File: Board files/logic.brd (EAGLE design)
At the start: 44.1 x 57.1 mm, 19 parts, among them U2 LD1117, U3 LM2662

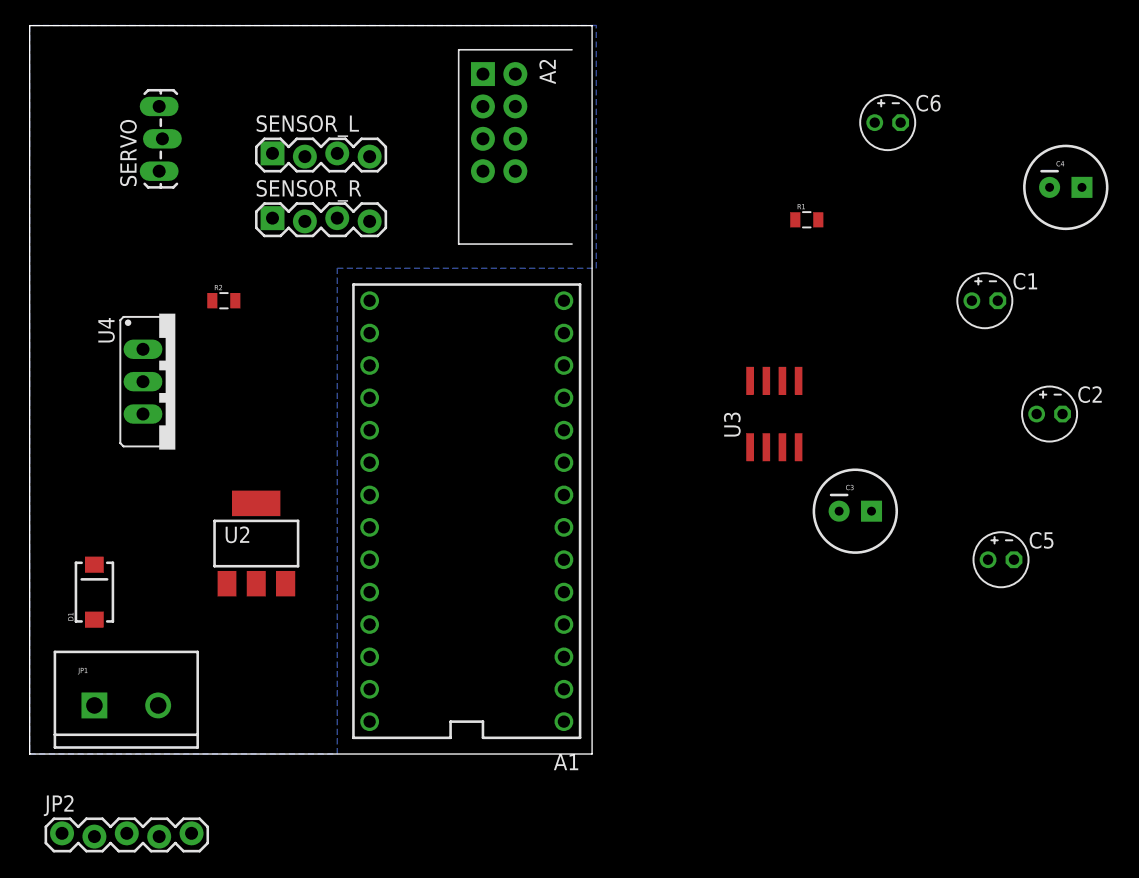
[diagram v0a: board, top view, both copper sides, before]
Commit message: Finished logic board layout
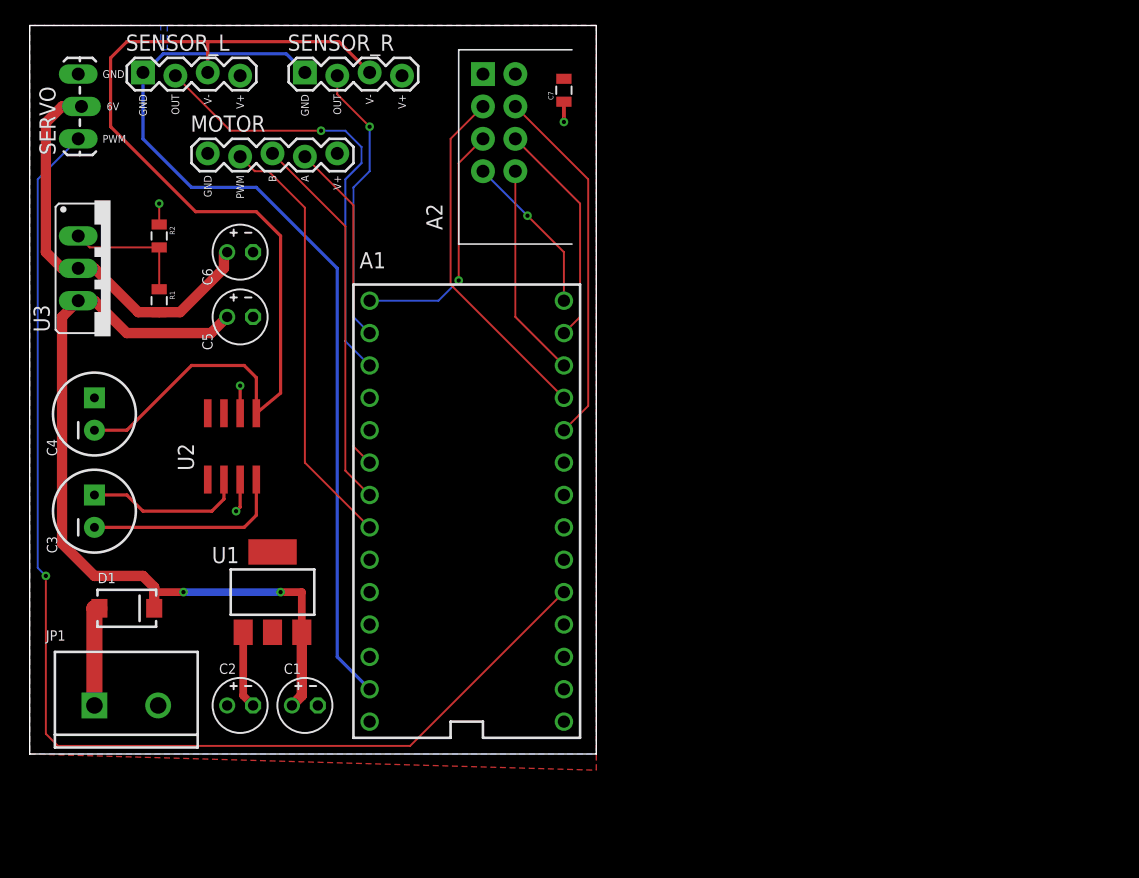
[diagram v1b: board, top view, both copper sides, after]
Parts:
- removed JP2: (no value), SparkFun-Connectors:1X05_LOCK
- removed U4: (no value), v-reg:317TS
- added C7: 0.1uF, SparkFun-Capacitors:0805
- added MOTOR: (no value), SparkFun-Connectors:1X05_LOCK
- added U1: LD1117, Custom:SOT-223
- C1, C2, C5, C6: value (none) -> 10uF
- C3, C4: value (none) -> 47uF
- U2: value LD1117 -> LM2662; device Custom:SOT-223 -> Custom:SOIC-8
- U3: value LM2662 -> LD1085V; device Custom:SOIC-8 -> v-reg:317TS
- moved C4 78.2 mm to (5.08, 26.7), turned to 90 degrees
- moved C2 67.5 mm to (16.5, 3.81)
- moved C5 62.7 mm to (16.5, 34.3)
- moved C1 62.1 mm to (21.6, 3.81)
- moved C3 59.7 mm to (5.08, 19.1), turned to 90 degrees
- moved U3 53.3 mm to (6.35, 38.1), turned to 270 degrees
- moved C6 51.8 mm to (16.5, 39.4)
- moved R1 51.2 mm to (10.2, 35.6), turned to 270 degrees
- moved SENSOR_L 12.0 mm to (8.89, 53.3)
- moved SENSOR_R 11.7 mm to (21.6, 53.3)
- moved U2 7.85 mm to (15.9, 24.1)
- moved R2 7.18 mm to (10.2, 40.6), turned to 270 degrees
- moved SERVO 6.84 mm to (3.81, 48.3)
- moved D1 2.84 mm to (7.62, 11.4), turned to 0 degrees
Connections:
- new net N$17: A1.18/A4, MOTOR.4
- net 3.3V: now also C7.2, MOTOR.5, U1.2, U1.4, U2.8; no longer JP2.5, U2.2, U2.4, U3.8
- net 6V: now also U3.2; no longer U4.2
- net GND: now also C7.1, MOTOR.1, U1.1, U2.3, U2.6; no longer A1.AGND, JP2.1, SENSOR_L.1, SENSOR_R.1, U2.1, U3.3, U3.6
- net N$10: now also A1.9; no longer A1.14/A0
- net N$12: now also A1.AGND, SENSOR_L.1, SENSOR_R.1; no longer A1.16/A2, SENSOR_R.2
- net N$13: now also A1.15/A1; no longer A1.17/A3
- net N$14: now also A1.14/A0, SENSOR_R.2; no longer A1.5, JP2.2
- net N$15: now also A1.20/A6, MOTOR.2; no longer A1.6, JP2.4
- net N$16: now also A1.19/A5, MOTOR.3; no longer A1.7, JP2.3
- net N$2: now also U2.2; no longer U3.2
- net N$3: now also U2.4; no longer U3.4
- net N$4: now also U3.1; no longer U4.1
- net N$8: now also A1.8; no longer A1.10
- net N$9: now also A1.10; no longer A1.15/A1
- net VNEG: now also U2.5; no longer U3.5
- net V_BATT: now also U1.3, U3.3; no longer U2.3, U4.3
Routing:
- net N$11: track 0.00 -> 94.3 mm, vias 0 -> 1
- net VNEG: track 0.00 -> 79.3 mm
- net N$12: track 0.00 -> 72.6 mm
- net V_BATT: track 0.00 -> 63.9 mm, vias 0 -> 2
- net N$13: track 0.00 -> 35.4 mm, vias 0 -> 1
- net N$15: track 0.00 -> 33.9 mm
- net 6V: track 0.00 -> 32.3 mm
- net N$16: track 0.00 -> 30.0 mm
- net N$8: track 0.00 -> 28.6 mm
- net N$10: track 0.00 -> 27.6 mm
- net N$17: track 0.00 -> 26.1 mm
- net N$14: track 0.00 -> 22.3 mm, vias 0 -> 1
- net N$5: track 0.00 -> 19.5 mm, vias 0 -> 1
- net N$7: track 0.00 -> 17.9 mm
- net N$9: track 0.00 -> 16.8 mm
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- added copper zone on layer 1, net 3.3V
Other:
- board size 44.1 x 57.1 mm -> 44.5 x 57.1 mm
- board text added: "6V"
- board text added: "A"
- board text added: "B"
- board text added: "GND"
- board text added: "OUT"
- board text added: "PWM"
- board text added: "V+"
- board text added: "V-"

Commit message: Rerouted servo trace and added labels
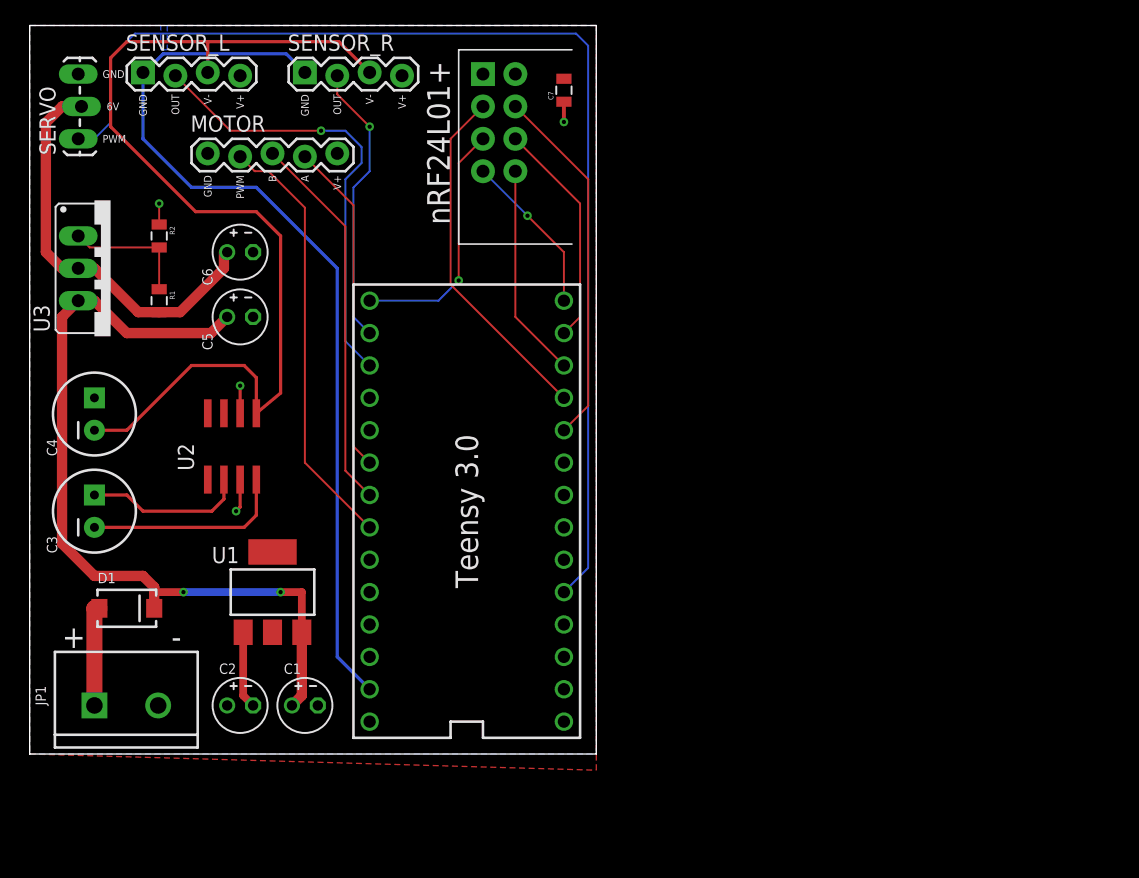
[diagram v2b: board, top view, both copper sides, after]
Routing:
- net N$11: track 94.3 -> 90.4 mm, vias 1 -> 0
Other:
- board text added: "+"
- board text added: "-"
- board text added: "Teensy 3.0"
- board text added: "nRF24L01+"
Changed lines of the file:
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@@
 <text x="26.67" y="51.7525" size="0.6096" layer="21" rot="R270" align="center-left">V-</text>
 <text x="29.21" y="51.7525" size="0.6096" layer="21" rot="R270" align="center-left">V+</text>
+<text x="2.54" y="9.2075" size="1.778" layer="21" align="center-left">+</text>
+<text x="11.1125" y="9.2075" size="1.778" layer="21" align="center-left">-</text>
+<text x="34.29" y="19.05" size="1.778" layer="21" rot="R90" align="center">Teensy 3.0</text>
+<text x="32.0675" y="47.9425" size="1.778" layer="21" rot="R90" align="center">nRF24L01+</text>
 </plain>
 <attributes>
@@
 </element>
 <element name="JP1" library="SparkFun-Connectors" package="SCREWTERMINAL-5MM-2" value="M025MM" x="5.08" y="3.81" smashed="yes">
-<attribute name="NAME" x="1.27" y="8.89" size="0.8128" layer="25"/>
+<attribute name="NAME" x="1.27" y="3.81" size="0.8128" layer="25" rot="R90"/>
 </element>
 <element name="U3" library="v-reg" package="317TS" value="LD1085V" x="6.35" y="38.1" smashed="yes" rot="R270">
@@
 <attribute name="NAME" x="14.351" y="36.7665" size="0.8128" layer="25" ratio="10" rot="R90"/>
 </element>
-<element name="A2" library="Custom" package="NRF24L01+" value="NRF24L01+" x="36.83" y="49.53" smashed="yes" rot="R270">
-<attribute name="NAME" x="31.115" y="43.18" size="1.27" layer="25" ratio="10" rot="R270"/>
-</element>
-<element name="A1" library="Teensy3.0" package="TEENSY_3.0_SIDES" value="TEENSY_3.0_SIDES" x="34.29" y="19.05" smashed="yes" rot="R180">
-<attribute name="NAME" x="27.94" y="39.37" size="1.27" layer="25" font="vector" rot="R180"/>
-</element>
+<element name="A2" library="Custom" package="NRF24L01+" value="NRF24L01+" x="36.83" y="49.53" smashed="yes" rot="R270"/>
+<element name="A1" library="Teensy3.0" package="TEENSY_3.0_SIDES" value="TEENSY_3.0_SIDES" x="34.29" y="19.05" smashed="yes" rot="R180"/>
 <element name="SERVO" library="SparkFun-Connectors" package="1X03_LOCK_LONGPADS" value="" x="3.81" y="48.26" smashed="yes" rot="R90">
 <attribute name="NAME" x="2.032" y="46.99" size="1.27" layer="25" font="vector" ratio="10" rot="R90"/>
@@
 <contactref element="SERVO" pad="1"/>
 <contactref element="A1" pad="3"/>
-<wire x1="3.81" y1="48.26" x2="0.635" y2="45.085" width="0.1524" layer="16"/>
-<wire x1="0.635" y1="45.085" x2="0.635" y2="14.605" width="0.1524" layer="16"/>
-<wire x1="0.635" y1="14.605" x2="1.27" y2="13.97" width="0.1524" layer="16"/>
-<via x="1.27" y="13.97" extent="1-16" drill="0.3302"/>
-<wire x1="1.27" y1="13.97" x2="1.27" y2="1.5875" width="0.1524" layer="1"/>
-<wire x1="1.27" y1="1.5875" x2="2.2225" y2="0.635" width="0.1524" layer="1"/>
-<wire x1="2.2225" y1="0.635" x2="29.845" y2="0.635" width="0.1524" layer="1"/>
-<wire x1="29.845" y1="0.635" x2="41.91" y2="12.7" width="0.1524" layer="1"/>
+<wire x1="41.91" y1="12.7" x2="43.815" y2="14.605" width="0.1524" layer="16"/>
+<wire x1="43.815" y1="14.605" x2="43.815" y2="55.5625" width="0.1524" layer="16"/>
+<wire x1="43.815" y1="55.5625" x2="42.8625" y2="56.515" width="0.1524" layer="16"/>
+<wire x1="42.8625" y1="56.515" x2="8.255" y2="56.515" width="0.1524" layer="16"/>
+<wire x1="8.255" y1="56.515" x2="6.35" y2="54.61" width="0.1524" layer="16"/>
+<wire x1="6.35" y1="54.61" x2="6.35" y2="49.53" width="0.1524" layer="16"/>
+<wire x1="6.35" y1="49.53" x2="5.08" y2="48.26" width="0.1524" layer="16"/>
+<wire x1="5.08" y1="48.26" x2="3.81" y2="48.26" width="0.1524" layer="16"/>
 </signal>
 <signal name="N$6">

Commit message: Changed logic board layout
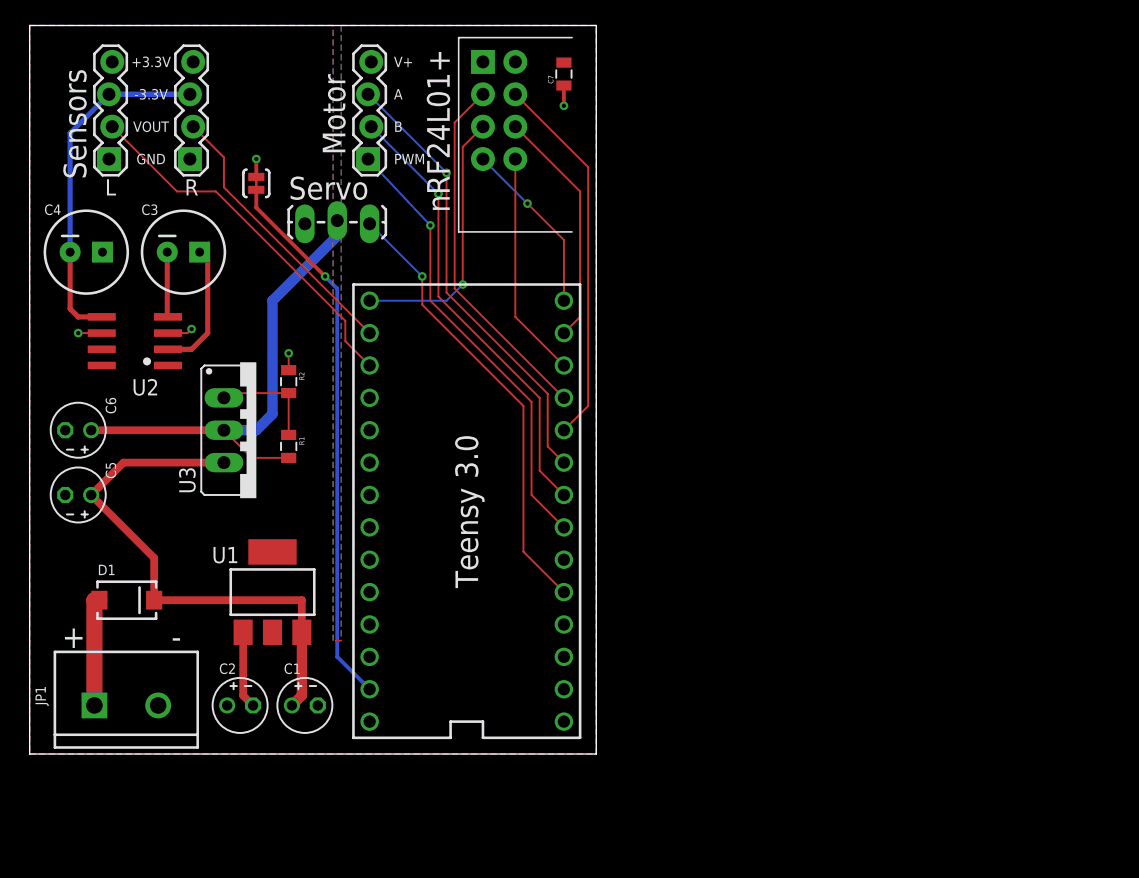
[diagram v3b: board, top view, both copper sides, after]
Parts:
- added SJ1: SOLDERJUMPERTRACE, SparkFun-Passives:SJ_2S-TRACE
- MOTOR: device SparkFun-Connectors:1X05_LOCK -> SparkFun-Connectors:1X04_LOCK
- moved SERVO 23.8 mm to (26.7, 41.6), turned to 180 degrees
- moved C3 21.5 mm to (12.1, 39.4), turned to 0 degrees
- moved C5 18.9 mm to (3.81, 20.3), turned to 180 degrees
- moved C6 18.9 mm to (3.81, 25.4), turned to 180 degrees
- moved U3 17.1 mm to (17.8, 25.4)
- moved R1 15.3 mm to (20.3, 24.1)
- moved R2 15.3 mm to (20.3, 29.2)
- moved C4 12.7 mm to (4.45, 39.4), turned to 0 degrees
- moved MOTOR 12.7 mm to (26.7, 46.7), turned to 90 degrees
- moved U2 11.2 mm to (8.26, 32.4), turned to 90 degrees
- moved SENSOR_R 11.1 mm to (12.7, 46.7), turned to 90 degrees
- moved SENSOR_L 7.13 mm to (6.35, 46.7), turned to 90 degrees
- moved C7 1.27 mm to (41.9, 53.3)
- moved A2 0.95 mm to (36.8, 50.5)
- moved D1 0.63 mm to (7.62, 12.1)
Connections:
- net 3.3V: now also MOTOR.4; no longer MOTOR.5
- net GND: now also SENSOR_L.1, SENSOR_R.1, SJ1.2; no longer MOTOR.1
- net N$12: now also SJ1.1; no longer SENSOR_L.1, SENSOR_R.1
- net N$15: now also A1.5, MOTOR.1; no longer A1.20/A6, MOTOR.2
- net N$16: now also A1.6, MOTOR.2; no longer A1.19/A5, MOTOR.3
- net N$17: now also A1.7, MOTOR.3; no longer A1.18/A4, MOTOR.4
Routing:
- net N$11: track 90.4 -> 35.2 mm, vias 0 -> 1
- net VNEG: track 79.3 -> 27.2 mm
- net N$12: track 72.6 -> 42.9 mm, vias 0 -> 1
- net V_BATT: track 63.9 -> 42.6 mm, vias 2 -> 0
- net N$3: track 15.9 -> 5.10 mm
- net N$17: track 26.1 -> 35.3 mm, vias 0 -> 1
- net N$13: track 35.4 -> 28.9 mm, vias 1 -> 0
- net 6V: track 32.3 -> 38.0 mm
- net N$16: track 30.0 -> 35.2 mm, vias 0 -> 1
- net N$2: track 12.6 -> 10.3 mm
- net N$4: track 10.0 -> 8.51 mm
- net N$5: track 19.5 -> 20.9 mm
- net N$15: track 33.9 -> 35.2 mm, vias 0 -> 1
- net N$9: track 16.8 -> 17.8 mm
- net N$8: track 28.6 -> 29.5 mm
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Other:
- board text added: "+3.3V"
- board text added: "-3.3V"
- board text added: "L"
- board text added: "Motor"
- board text added: "R"
- board text added: "Sensors"
- board text added: "Servo"
- board text added: "VOUT"
- board text removed: "6V"
- board text removed: "OUT"
- board text removed: "V-"

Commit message: More logic board edits
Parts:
- moved U1 1.27 mm to (17.8, 12.7)
- moved C5 0.95 mm to (3.81, 21.3)
- moved C6 0.64 mm to (3.81, 26.0)
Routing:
- net V_BATT: track 42.6 -> 40.3 mm
- net GND: track 14.2 -> 14.7 mm
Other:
- board text added: "3.3V"
- board text removed: "V+"
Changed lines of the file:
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@@
 <text x="28.575" y="49.2125" size="0.8128" layer="21" align="center-left">B</text>
 <text x="28.575" y="51.7525" size="0.8128" layer="21" align="center-left">A</text>
-<text x="28.575" y="54.2925" size="0.8128" layer="21" align="center-left">V+</text>
+<text x="28.575" y="54.2925" size="0.8128" layer="21" align="center-left">3.3V</text>
 <text x="2.54" y="9.2075" size="1.778" layer="21" align="center-left">+</text>
 <text x="11.1125" y="9.2075" size="1.778" layer="21" align="center-left">-</text>
@@
 <attribute name="VALUE" x="7.874" y="13.716" size="0.4064" layer="27"/>
 </element>
-<element name="U1" library="Custom" package="SOT-223" value="LD1117" x="19.05" y="12.7" smashed="yes">
-<attribute name="NAME" x="14.2875" y="14.9733" size="1.27" layer="25"/>
+<element name="U1" library="Custom" package="SOT-223" value="LD1117" x="17.78" y="12.7" smashed="yes">
+<attribute name="NAME" x="13.0175" y="14.9733" size="1.27" layer="25"/>
 </element>
 <element name="JP1" library="SparkFun-Connectors" package="SCREWTERMINAL-5MM-2" value="M025MM" x="5.08" y="3.81" smashed="yes">
@@
 <attribute name="NAME" x="14.859" y="6.2865" size="0.8128" layer="25" ratio="10"/>
 </element>
-<element name="C5" library="resistor" package="E2-4" value="10uF" x="3.81" y="20.32" smashed="yes" rot="R180">
-<attribute name="NAME" x="5.969" y="22.9235" size="0.8128" layer="25" ratio="10" rot="R270"/>
-</element>
-<element name="C6" library="resistor" package="E2-4" value="10uF" x="3.81" y="25.4" smashed="yes" rot="R180">
-<attribute name="NAME" x="5.969" y="28.0035" size="0.8128" layer="25" ratio="10" rot="R270"/>
+<element name="C5" library="resistor" package="E2-4" value="10uF" x="3.81" y="21.2725" smashed="yes" rot="R180">
+<attribute name="NAME" x="5.969" y="23.876" size="0.8128" layer="25" ratio="10" rot="R270"/>
+</element>
+<element name="C6" library="resistor" package="E2-4" value="10uF" x="3.81" y="26.035" smashed="yes" rot="R180">
+<attribute name="NAME" x="5.969" y="28.6385" size="0.8128" layer="25" ratio="10" rot="R270"/>
 </element>
 <element name="A2" library="Custom" package="NRF24L01+" value="NRF24L01+" x="36.83" y="50.4825" smashed="yes" rot="R270"/>
@@
 <vertex x="0" y="57.15"/>
 </polygon>
-<wire x1="16.75" y1="9.55" x2="16.75" y2="4.586" width="0.6096" layer="1"/>
-<wire x1="16.75" y1="4.586" x2="17.526" y2="3.81" width="0.6096" layer="1"/>
 <contactref element="A2" pad="1"/>
 <contactref element="C7" pad="1"/>
@@
 <wire x1="17.78" y1="45.2755" x2="17.78" y2="46.6725" width="0.3048" layer="1"/>
 <via x="17.78" y="46.6725" extent="1-16" drill="0.3302"/>
+<wire x1="15.48" y1="9.55" x2="15.48" y2="7.38" width="0.6096" layer="1"/>
+<wire x1="15.48" y1="7.38" x2="17.526" y2="5.334" width="0.6096" layer="1"/>
+<wire x1="17.526" y1="5.334" x2="17.526" y2="3.81" width="0.6096" layer="1"/>
 </signal>
 <signal name="3.3V">
@@
 <contactref element="C1" pad="+"/>
 <contactref element="C5" pad="+"/>
-<wire x1="21.35" y1="9.55" x2="21.35" y2="8.89" width="0.8128" layer="1"/>
-<wire x1="21.35" y1="8.89" x2="21.35" y2="4.586" width="0.8128" layer="1"/>
-<wire x1="21.35" y1="4.586" x2="20.574" y2="3.81" width="0.8128" layer="1"/>
-<wire x1="9.77" y1="12.065" x2="9.77" y2="15.376" width="0.6096" layer="1"/>
-<wire x1="9.77" y1="15.376" x2="4.826" y2="20.32" width="0.6096" layer="1"/>
-<wire x1="15.24" y1="22.86" x2="7.366" y2="22.86" width="0.6096" layer="1"/>
-<wire x1="7.366" y1="22.86" x2="4.826" y2="20.32" width="0.6096" layer="1"/>
-<wire x1="9.77" y1="12.065" x2="21.35" y2="12.065" width="0.6096" layer="1"/>
-<wire x1="21.35" y1="12.065" x2="21.35" y2="8.89" width="0.6096" layer="1"/>
+<wire x1="9.77" y1="12.065" x2="9.77" y2="16.3285" width="0.8128" layer="1"/>
+<wire x1="20.08" y1="9.55" x2="20.08" y2="4.304" width="0.6096" layer="1"/>
+<wire x1="20.08" y1="4.304" x2="20.574" y2="3.81" width="0.6096" layer="1"/>
+<wire x1="9.77" y1="12.065" x2="18.415" y2="12.065" width="0.6096" layer="1"/>
+<wire x1="18.415" y1="12.065" x2="20.32" y2="10.16" width="0.6096" layer="1"/>
+<wire x1="20.32" y1="10.16" x2="20.32" y2="9.79" width="0.6096" layer="1"/>
+<wire x1="20.32" y1="9.79" x2="20.08" y2="9.55" width="0.6096" layer="1"/>
+<wire x1="9.77" y1="16.3285" x2="4.826" y2="21.2725" width="0.8128" layer="1"/>
+<wire x1="4.826" y1="21.2725" x2="13.6525" y2="21.2725" width="0.8128" layer="1"/>
+<wire x1="13.6525" y1="21.2725" x2="15.24" y2="22.86" width="0.8128" layer="1"/>
 </signal>
 <signal name="N$1">
@@
 <wire x1="20.32" y1="23.23" x2="17.41" y2="23.23" width="0.1524" layer="1"/>
 <wire x1="17.41" y1="23.23" x2="15.24" y2="25.4" width="0.1524" layer="1"/>
-<wire x1="4.826" y1="25.4" x2="15.24" y2="25.4" width="0.6096" layer="1"/>
+<wire x1="4.826" y1="26.035" x2="5.461" y2="25.4" width="0.8128" layer="1"/>
+<wire x1="5.461" y1="25.4" x2="15.24" y2="25.4" width="0.8128" layer="1"/>
 </signal>
 <signal name="N$4">
